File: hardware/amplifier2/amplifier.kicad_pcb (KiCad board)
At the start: 2 copper layers, 92 x 82 mm, 128 parts, among them IC1 AD8331, IC2 ISL55210, IC3 LP38798, IC4 NC7SVU04, IC5 LTC2252, J1 0, P1 5V, P2 UART, P4 VGA - LNA, P5 LNA - SDR, SW1 SW_PUSH, T1 BALUN, T2 BALUN, T3 BALUN, T4 BALUN, U1 MCP4706/16/26, X1 IN_AD, X2 IN_FILTER, X3 OUT_FILTER, X4 IN_ADC, X5 IN_ISL, X6 OUT_ISL, X7 OUT_AD, Y1 FVXO-HC53BR

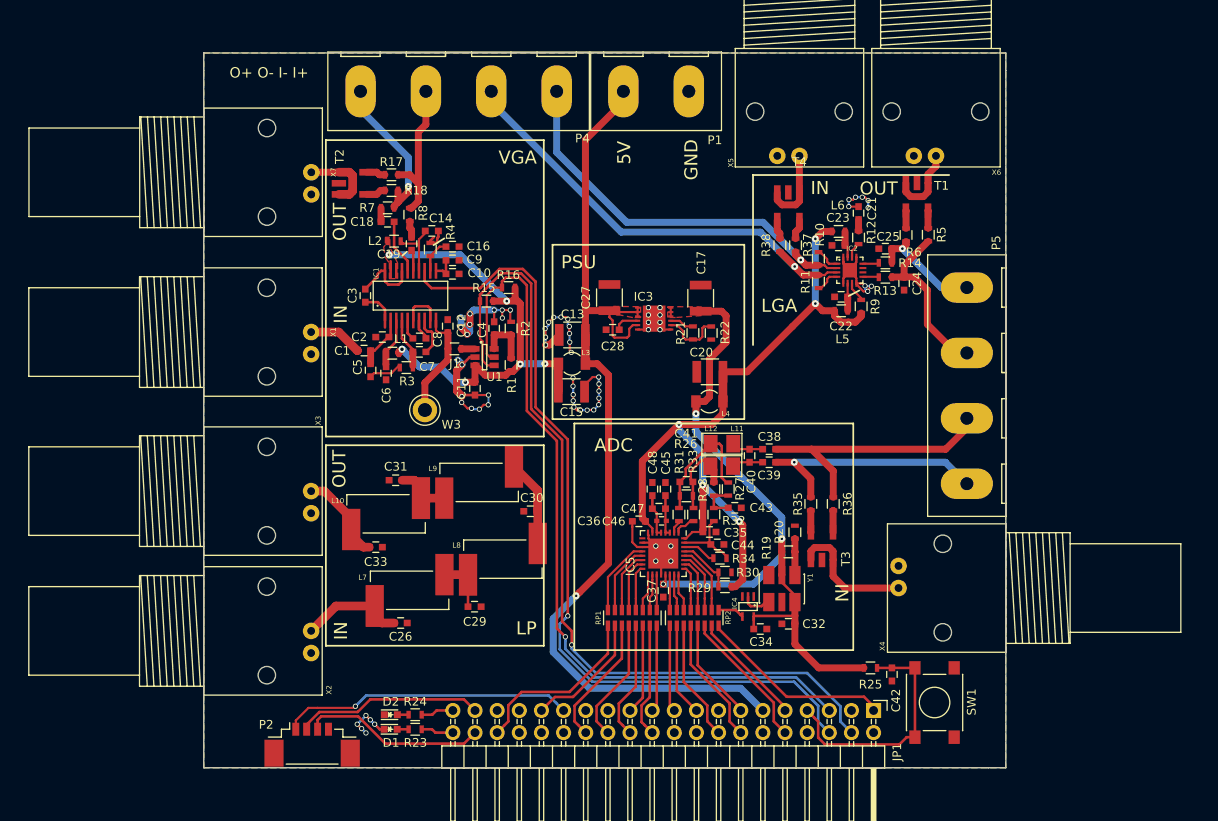
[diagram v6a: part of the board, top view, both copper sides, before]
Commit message: checked groundplane; added ground viastitching where necessary; added slits in groundplane where necessary; added mounting holes; adjusted silkscreen; adjusted board outline
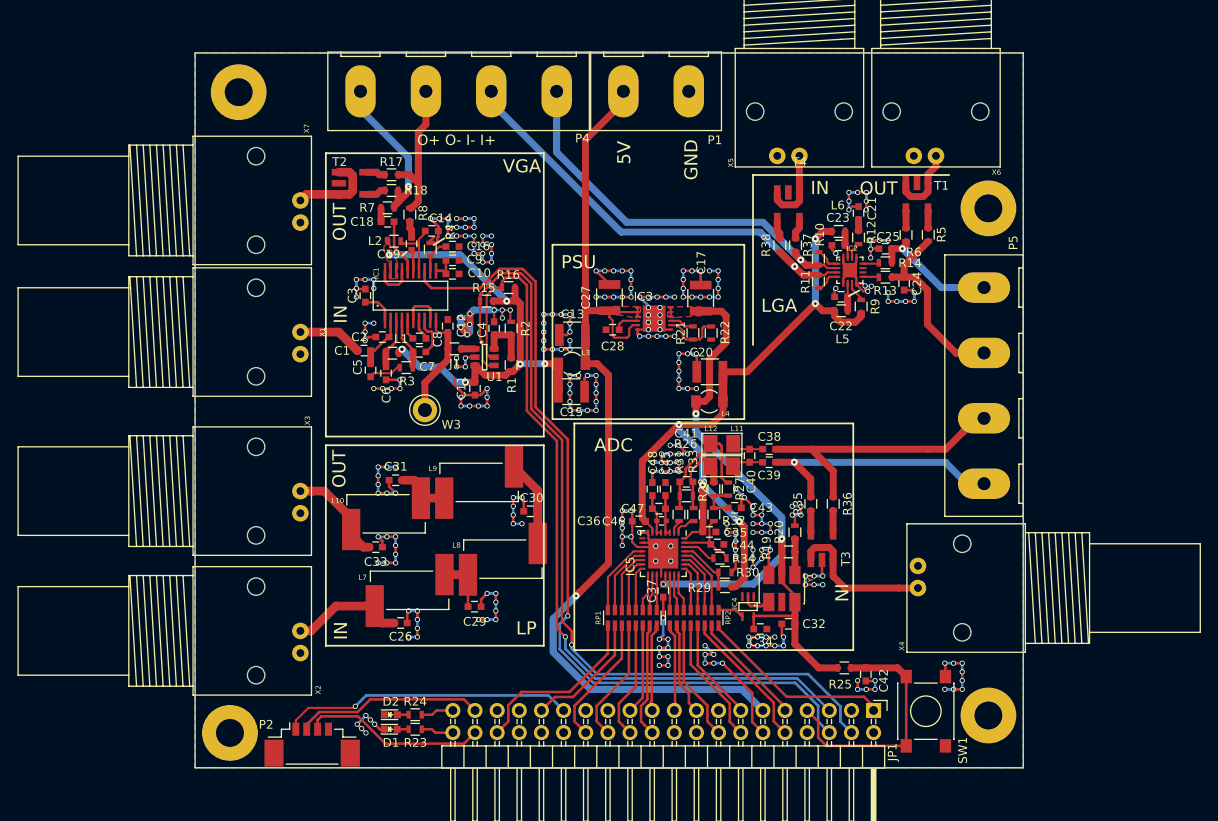
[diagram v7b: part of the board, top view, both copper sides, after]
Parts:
- added M1: MountingHole_3.2mm_M3_Pad, Mounting_Holes:MountingHole_3.2mm_M3_Pad, F.Cu at (120.0, 120.8)
- added M2: MountingHole_3.2mm_M3_Pad, Mounting_Holes:MountingHole_3.2mm_M3_Pad, F.Cu at (120.0, 179.0)
- added M3: MountingHole_3.2mm_M3_Pad, Mounting_Holes:MountingHole_3.2mm_M3_Pad, F.Cu at (33.0, 181.0)
- added M4: MountingHole_3.2mm_M3_Pad, Mounting_Holes:MountingHole_3.2mm_M3_Pad, F.Cu at (34.0, 107.5)
- moved X7 3.46 mm to (41.1, 122.5)
- moved C42 3.00 mm to (105.9, 174.3)
- moved R25 3.00 mm to (103.5, 173.5)
- moved X4 2.23 mm to (111.9, 161.8)
- moved P5 1.97 mm to (119.5, 141.2)
- moved SW1 1.41 mm to (112.8, 178.5)
- moved X1 1.23 mm to (41.1, 137.6)
- moved X2 1.23 mm to (41.1, 171.8)
- moved X3 1.23 mm to (41.1, 155.8)
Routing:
- net GNDA: track 112.1 -> 368.9 mm, vias 68 -> 301
- net +3V3: track 116.6 -> 113.6 mm
- net Net-(T3-Pad1): track 14.8 -> 17.1 mm
- net /OUT1-: track 20.8 -> 23.1 mm
- net /IN3-: track 30.6 -> 32.6 mm
- net /OUT1+: track 13.1 -> 15.1 mm
- net /IN3+: track 27.8 -> 29.7 mm
- net Net-(T2-Pad1): track 8.42 -> 9.95 mm
- net Net-(C33-Pad1): track 10.7 -> 11.9 mm
- net Net-(C26-Pad1): track 12.2 -> 13.4 mm
- net Net-(C1-Pad2): track 6.20 -> 7.43 mm
- net /SW1: track 27.7 -> 28.8 mm
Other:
- board size 92 x 82 mm -> 95 x 82 mm

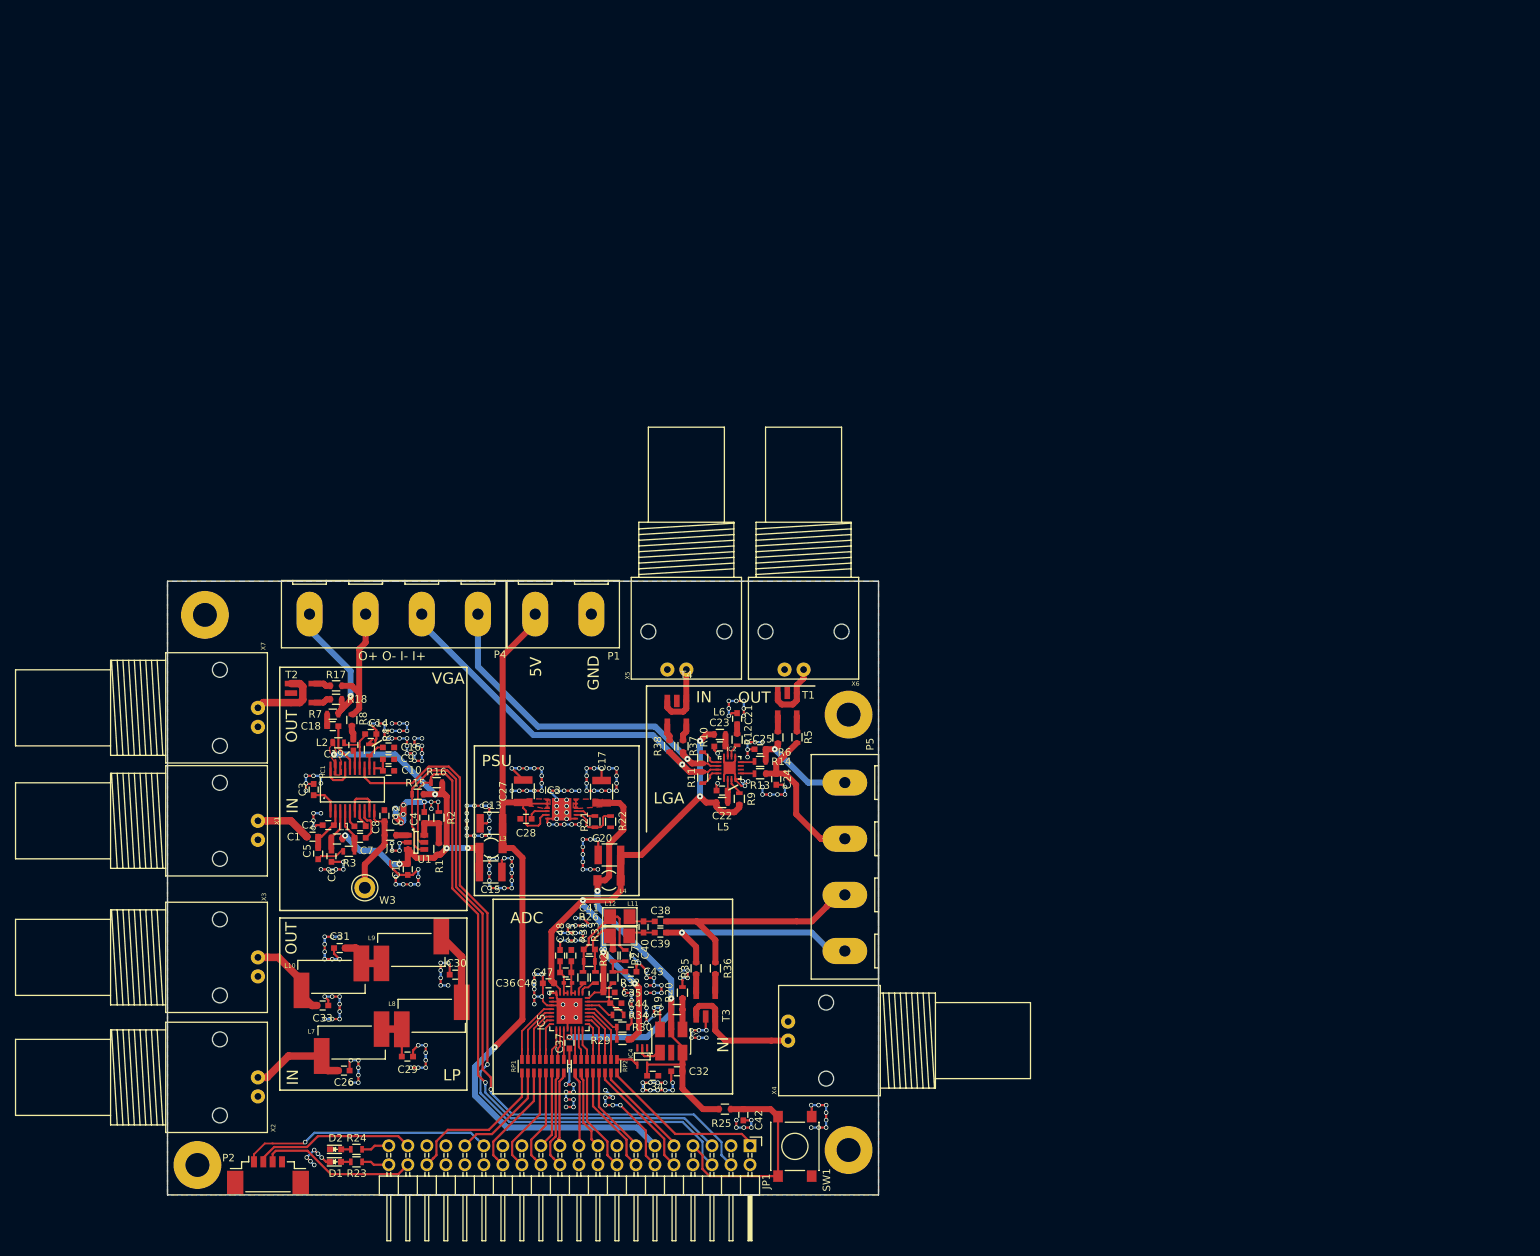
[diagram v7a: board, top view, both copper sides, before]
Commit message: Added notes to schematic explaining some of the features; Adjusted dimension markers of the board
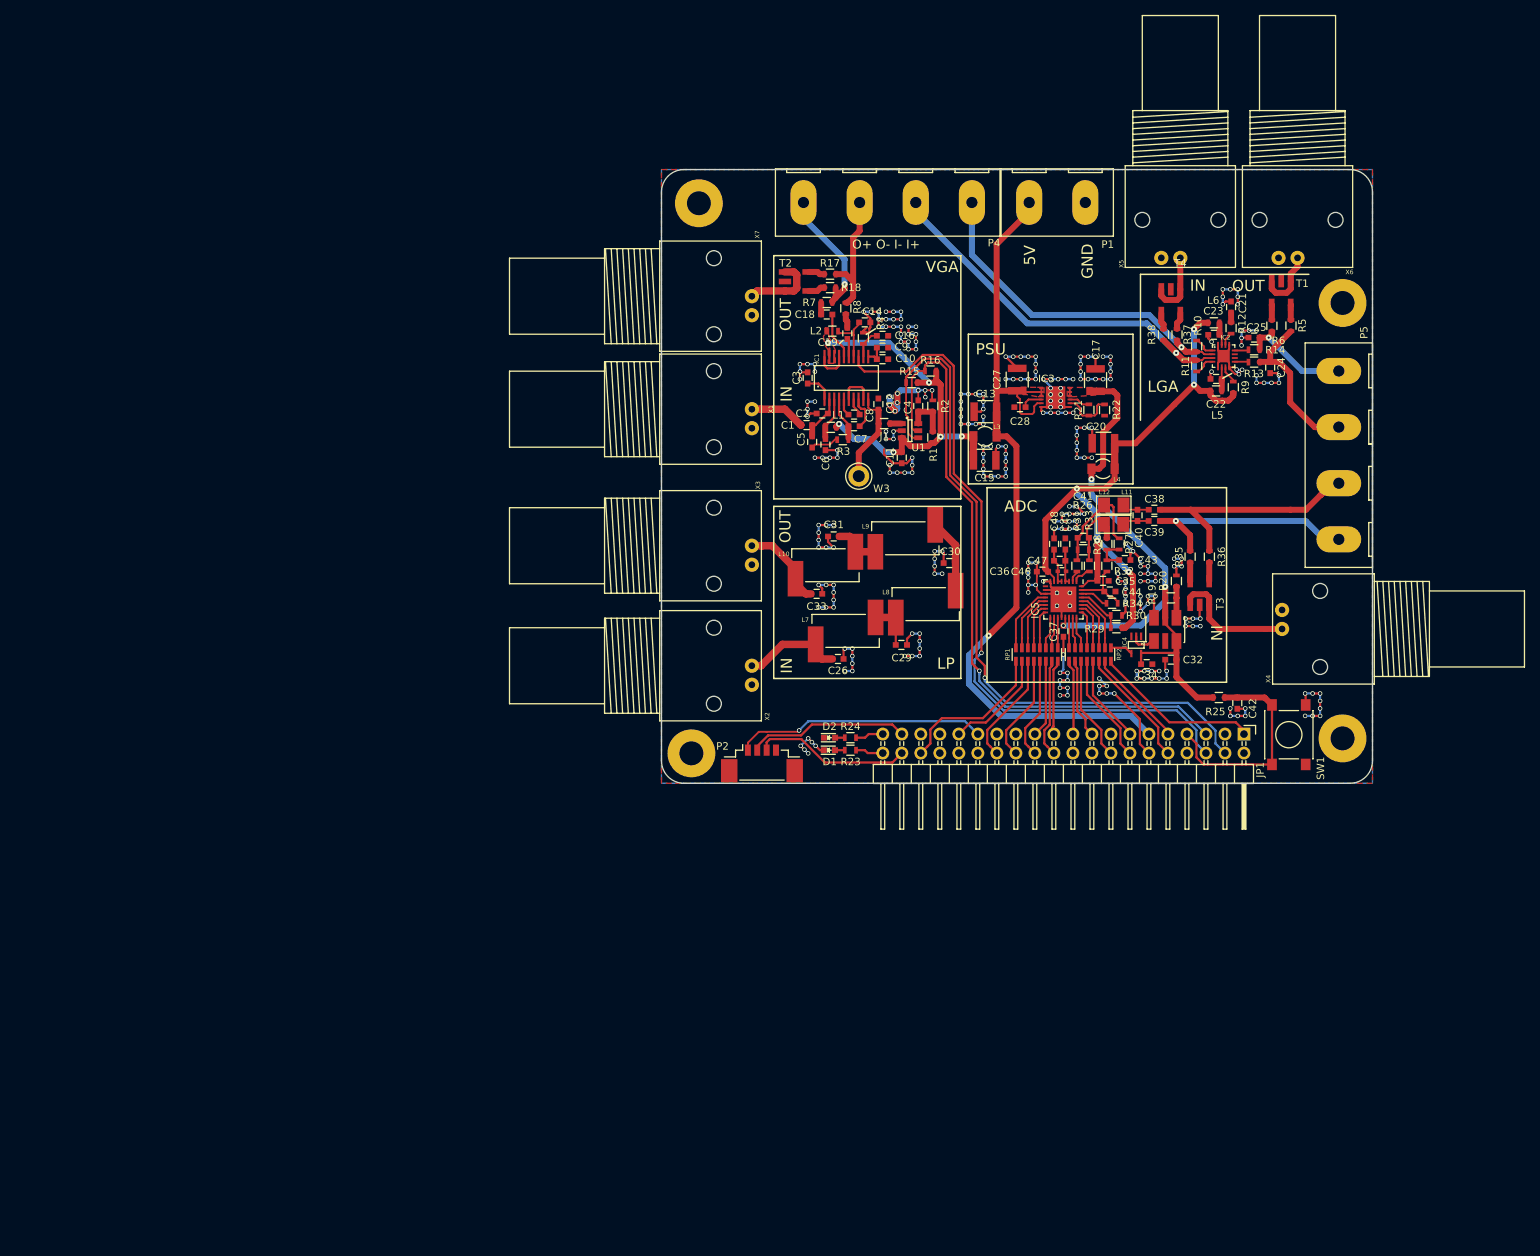
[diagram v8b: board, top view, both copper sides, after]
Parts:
- moved C28 85.9 mm to (142.9, 79.7)
- moved C34 85.9 mm to (159.8, 114.1)
- moved C37 85.9 mm to (148.7, 109.7)
- moved IC5 85.9 mm to (148.7, 105.4)
- moved JP1 85.9 mm to (172.8, 123.4)
- moved C10 85.9 mm to (124.5, 73.3)
- moved C11 85.9 mm to (127.1, 86.5)
- moved C12 85.9 mm to (124.0, 79.3)
- moved C13 85.9 mm to (138.3, 80.3)
- moved C14 85.9 mm to (122.2, 68.4)
- moved C15 85.9 mm to (138.2, 86.8)
- moved C16 85.9 mm to (124.5, 70.2)
- moved C17 85.9 mm to (153.0, 76.1)
- moved C18 85.9 mm to (117.1, 67.4)
- moved C19 85.9 mm to (119.8, 69.9)
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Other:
- outline, holes or cut-outs redrawn
